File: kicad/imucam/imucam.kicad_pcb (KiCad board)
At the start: 4 copper layers, 52.3 x 76.2 mm, 158 parts, among them J1 JTAG, J2 EXTCAM, J3 NUCLEO_CN8, J4 NUCLEO_CN9, J5 NUCLEO_CN7, J6 NUCLEO_CN10, J7 HDMI, Q1 BSS214NW, Q2 BSS214NW, Q3 BSS214NW, Q4 BSS214NW, U1 TLV73310PDBVT, U10 NTS0308E, U11 PTN3366, U12 AP2331, U2 LIFCL-17-xSG72, U3 AT25SF081-SSHD-X, U4 MIC5365-2.8YD5, U5 AR0330CM1C00, U6 ICM20948, U7 TPS562200, U8 INA219AxDCN, U9 TPS562200, X1 ECS-2520MV-xxx-xx

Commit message: Ready to begin routing differential pairs
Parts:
- C1, C10, C12, C13, C14, C15, C16, C17, C18, C19, C20, C21, C22, C23, C24, C25, C26, C27, C28, C29, C3, C30, C31, C32, C33, C34, C4, C40, C41, C42, C43, C44, C45, C46, C47, C48, C49, C5, C50, C51, C52, C53, C6, C7, C74, C75, C9, FB1, FB2, FB3, FB4: moved to B.Cu
- U11: footprint Package_DFN_QFN:QFN-32-1EP_5x5mm_P0.5mm_EP3.6x3.6mm_ThermalVias -> Package_DFN_QFN:QFN-32-1EP_5x5mm_P0.5mm_EP3.6x3.6mm
- U2: footprint Package_DFN_QFN:QFN-72-1EP_10x10mm_P0.5mm_EP6x6mm_ThermalVias -> Package_DFN_QFN:QFN-72-1EP_10x10mm_P0.5mm_EP6x6mm
- U6: footprint Package_DFN_QFN:QFN-24-1EP_3x3mm_P0.4mm_EP1.75x1.6mm -> imucam:QFN-24-1EP_3x3mm_P0.4mm_EP1.75x1.6mm_NoDiePad
- moved C23 216.3 mm to (27.1, 62.5), turned to 180 degrees
- moved C22 205.5 mm to (21.4, 61.9), turned to 90 degrees
- moved C30 162.7 mm to (27.1, 58.5), turned to 180 degrees
- moved C1 160.0 mm to (27.1, 59.5), turned to 180 degrees
- moved C19 151.1 mm to (27.4, 53.0), turned to 180 degrees
- moved C24 149.2 mm to (22.8, 64.3)
- moved C3 147.4 mm to (27.1, 56.6), turned to 180 degrees
- moved C27 145.9 mm to (24.4, 55.2), turned to 270 degrees
- moved R27 145.7 mm to (6.71, 2.62)
- moved C9 144.4 mm to (25.8, 63.8), turned to 180 degrees
- moved C13 143.1 mm to (21.0, 55.2), turned to 270 degrees
- moved C26 141.8 mm to (27.4, 55.0), turned to 270 degrees
- moved C12 141.4 mm to (29.0, 57.7), turned to 90 degrees
- moved C25 139.8 mm to (27.1, 60.5), turned to 180 degrees
- moved C6 139.8 mm to (24.1, 60.8), turned to 90 degrees
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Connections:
- net Net-(C11-Pad1) renamed /FPGA/1V8A_PHY
- net Net-(C15-Pad1) renamed /FPGA/1V0A_PHY
- net Net-(C30-Pad1) renamed /FPGA/1V8A
- net Net-(C4-Pad1) renamed /FPGA/1V0A_PLL
- net Net-(C66-Pad1) renamed /hdmi/IN_D1+
- net Net-(C67-Pad1) renamed /hdmi/IN_D2+
- net Net-(C68-Pad1) renamed /hdmi/IN_D3+
- net Net-(C69-Pad1) renamed /hdmi/IN_D4+
- net Net-(C70-Pad1) renamed /hdmi/IN_D1-
- net Net-(C71-Pad1) renamed /hdmi/IN_D2-
- net Net-(C72-Pad1) renamed /hdmi/IN_D3-
- net Net-(C73-Pad1) renamed /hdmi/IN_D4-
- J3 pad 10: (no net) -> /nucleo/LED3
- J3 pad 6: (no net) -> /nucleo/LED1
- J3 pad 8: (no net) -> /nucleo/LED2
- J4 pad 14: (no net) -> /nucleo/IMU_SCK_3V3
- J4 pad 16: CAM_RESET_BAR -> /nucleo/IMU_CS_3V3
- J4 pad 18: (no net) -> /nucleo/IMU_SO_3V3
- J4 pad 19: HDMI_SCL -> SCL_3V3
- J4 pad 20: (no net) -> /nucleo/IMU_SI_3V3
- J4 pad 21: HDMI_SDA -> SDA_3V3
- J4 pad 22: (no net) -> /nucleo/IMU_INT_3V3
- J4 pad 24: HDMI_HPD -> (no net)
- J4 pad 26: HDMI_OE -> (no net)
- J4 pad 28: HDMI_DDC_EN -> (no net)
- J4 pad 29: HDMI_EQ0 -> (no net)
- J4 pad 30: HDMI_EQ1 -> (no net)
- J5 pad 11: /nucleo/IMU_INT_3V3 -> (no net)
- J5 pad 13: /nucleo/IMU_SI_3V3 -> (no net)
- J5 pad 15: /nucleo/IMU_SCK_3V3 -> (no net)
- J5 pad 17: /nucleo/IMU_CS_3V3 -> (no net)
- J5 pad 19: /nucleo/IMU_SO_3V3 -> (no net)
- J5 pad 2: SCL_3V3 -> (no net)
- J5 pad 4: SDA_3V3 -> (no net)
- J6 pad 12: (no net) -> HDMI_SDA
- J6 pad 13: (no net) -> HDMI_OE
- J6 pad 15: (no net) -> HDMI_DDC_EN
- J6 pad 19: /nucleo/LED3 -> HDMI_EQ0
- J6 pad 2: (no net) -> CAM_RESET_BAR
- J6 pad 21: /nucleo/LED2 -> HDMI_HPD
- J6 pad 23: /nucleo/LED1 -> HDMI_EQ1
- J6 pad 8: (no net) -> HDMI_SCL
- R18 pad 1: +5V -> /nucleo/5V_IN
- R18 pad 2: /nucleo/5V_IN -> +5V
- U10 pad 11: (no net) -> GND
- U2 pad 10: HDMI_D2_N -> HDMI_D2_P
- U2 pad 11: HDMI_D2_P -> HDMI_D2_N
- U2 pad 13: HDMI_D1_N -> HDMI_D1_P
- U2 pad 14: HDMI_D1_P -> HDMI_D1_N
- U2 pad 15: HDMI_D0_N -> HDMI_D0_P
- U2 pad 16: HDMI_D0_P -> HDMI_D0_N
- U3 pad 3: +3V3 -> (no net)
- U3 pad 7: +3V3 -> (no net)
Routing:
- net GND: track 0.00 -> 58.3 mm, vias 0 -> 17
- net +1V0: track 0.00 -> 39.8 mm, vias 0 -> 5
- net /FPGA/1V8A: track 0.00 -> 25.4 mm, vias 0 -> 4
- net +1V8: track 0.81 -> 23.2 mm, vias 0 -> 9
- net HDMI_D2_P: track 0.00 -> 15.4 mm
- net HDMI_D2_N: track 0.00 -> 14.8 mm
- net HDMI_D1_P: track 0.00 -> 12.6 mm
- net HDMI_D1_N: track 0.00 -> 12.0 mm
- net +2V8: track 0.00 -> 11.7 mm, vias 0 -> 3
- net HDMI_D0_P: track 0.00 -> 10.2 mm
- net HDMI_D0_N: track 0.00 -> 9.65 mm
- net +3V3: track 0.00 -> 9.00 mm, vias 0 -> 4
- net HDMI_CK_P: track 0.00 -> 7.72 mm
- net HDMI_CK_N: track 0.00 -> 7.43 mm
- net /FPGA/1V0A_PHY: track 0.00 -> 5.81 mm, vias 0 -> 1
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
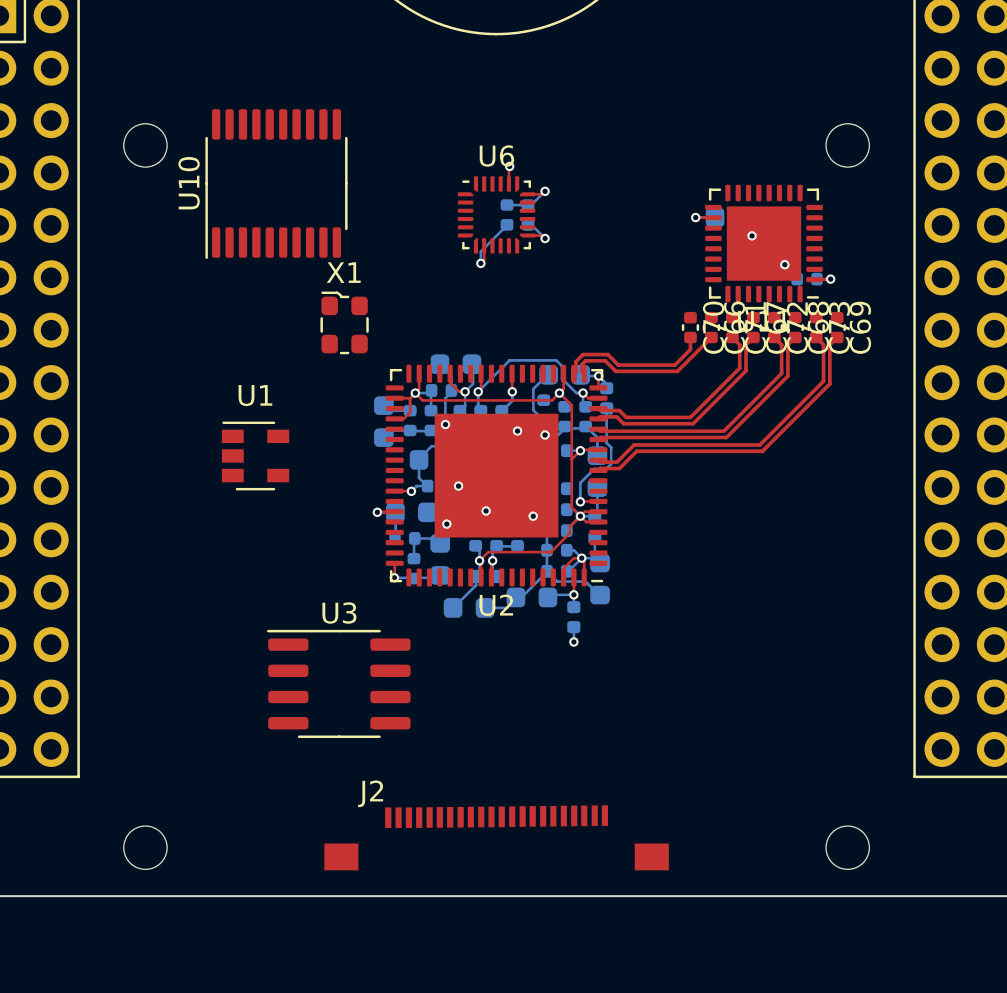
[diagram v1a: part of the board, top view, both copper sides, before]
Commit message: Routed first differential pairs
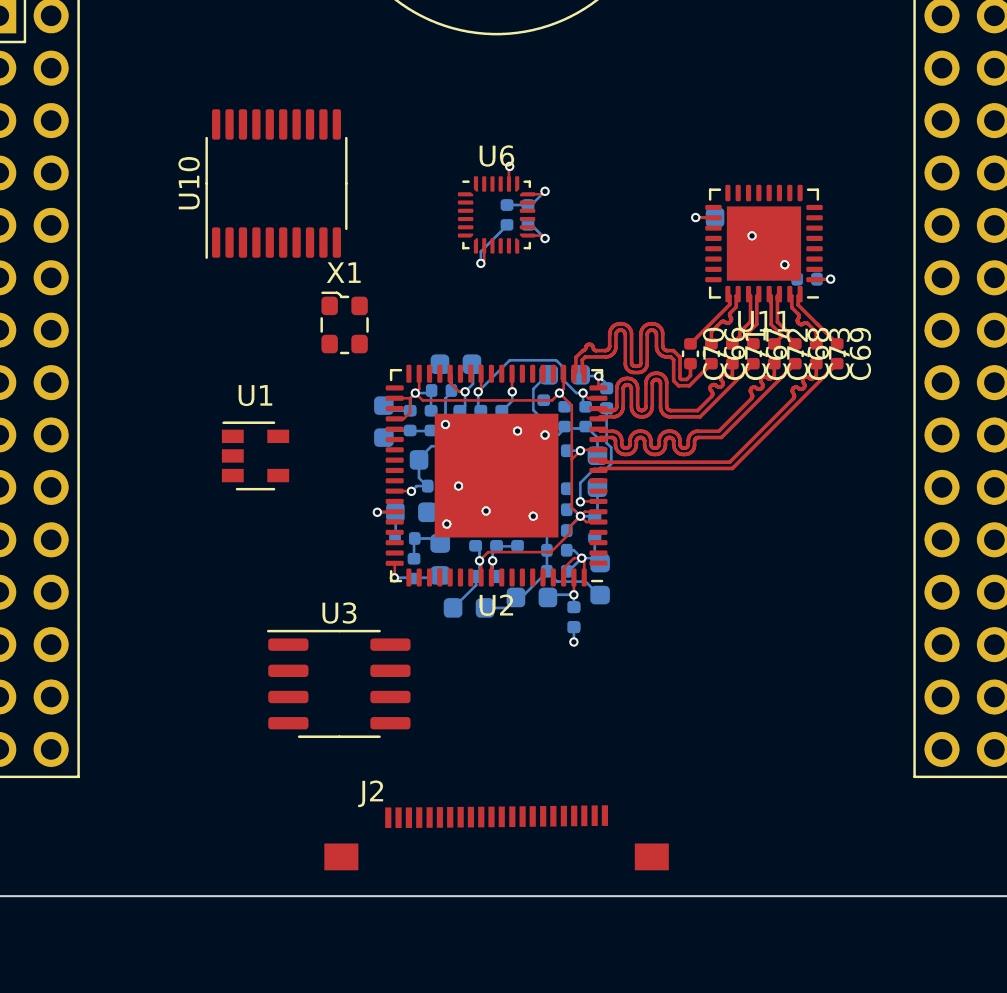
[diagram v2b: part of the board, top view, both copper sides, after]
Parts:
- removed H2: EXTCAM, imucam:Arducam_module_40mm
- moved C66 1.27 mm to (34.5, 51.9)
- moved C67 1.27 mm to (36.6, 51.9)
- moved C68 1.27 mm to (38.6, 51.9)
- moved C69 1.27 mm to (40.6, 51.9)
- moved C70 1.27 mm to (33.5, 51.9)
- moved C71 1.27 mm to (35.6, 51.9)
- moved C72 1.27 mm to (37.6, 51.9)
- moved C73 1.27 mm to (39.6, 51.9)
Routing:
- net HDMI_CK_N: track 7.43 -> 14.2 mm
- net HDMI_CK_P: track 7.72 -> 14.2 mm
- net HDMI_D0_N: track 9.65 -> 14.5 mm
- net HDMI_D0_P: track 10.2 -> 14.2 mm
- net /hdmi/IN_D1+: track 0.00 -> 3.29 mm
- net /hdmi/IN_D4-: track 0.00 -> 3.29 mm
- net /hdmi/IN_D1-: track 0.00 -> 3.24 mm
- net /hdmi/IN_D4+: track 0.00 -> 3.24 mm
- net /hdmi/IN_D3-: track 0.00 -> 3.13 mm
- net /hdmi/IN_D3+: track 0.00 -> 3.00 mm
- net /hdmi/IN_D2+: track 0.00 -> 2.82 mm
- net /hdmi/IN_D2-: track 0.00 -> 2.82 mm
- net HDMI_D1_N: track 12.0 -> 14.3 mm
- net HDMI_D1_P: track 12.6 -> 14.3 mm
- net HDMI_D2_P: track 15.4 -> 13.7 mm
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
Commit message: More routing
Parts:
- added H2: EXTCAM, imucam:Arducam_module_40mm, F.Cu at (24.1, 57.3)
- C35, C36, C37, C54, C62, C65, FB5, R31, R32, R33, R34, R35, R36, R37, R38, R39: moved to B.Cu
- moved R11 269.7 mm to (64.8, 44.5)
- moved R12 186.9 mm to (-19.3, 57.6), turned to 180 degrees
- moved C65 149.0 mm to (6.73, 55.5), turned to 90 degrees
- moved C37 84.9 mm to (16.8, 49.8)
- moved C36 84.2 mm to (16.8, 51.2)
- moved FB5 84.2 mm to (16.8, 48.8)
- moved C35 80.9 mm to (16.0, 67.6), turned to 270 degrees
- moved R39 59.0 mm to (27.6, 14.9), turned to 180 degrees
- moved C62 50.0 mm to (7.75, 55.5), turned to 270 degrees
- moved R34 41.6 mm to (34.7, 47.1), turned to 270 degrees
- moved C54 41.3 mm to (24.6, 45.2), turned to 90 degrees
- moved R31 35.2 mm to (39.2, 45.3), turned to 0 degrees
- moved R35 32.0 mm to (39.2, 44.3), turned to 0 degrees
- moved R38 31.8 mm to (27.1, 15.9), turned to 180 degrees
- moved R36 31.3 mm to (39.2, 49.3), turned to 0 degrees
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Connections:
- J6 pad 13: HDMI_OE -> HDMI_EQ0
- J6 pad 15: HDMI_DDC_EN -> HDMI_EQ1
- J6 pad 19: HDMI_EQ0 -> HDMI_HPD
- J6 pad 21: HDMI_HPD -> HDMI_DDC_EN
- J6 pad 23: HDMI_EQ1 -> HDMI_OE
- R25 pad 1: SDA_1V8 -> SCL_1V8
- R26 pad 1: SCL_1V8 -> SDA_1V8
- R29 pad 2: SCL_3V3 -> SDA_3V3
- R30 pad 2: SDA_3V3 -> SCL_3V3
- U10 pad 1: SCL_1V8 -> SDA_1V8
- U10 pad 13: /nucleo/IMU_SI_3V3 -> /nucleo/IMU_SCK_3V3
- U10 pad 14: /nucleo/IMU_SO_3V3 -> /nucleo/IMU_CS_3V3
- U10 pad 15: /nucleo/IMU_CS_3V3 -> /nucleo/IMU_SO_3V3
- U10 pad 16: /nucleo/IMU_SCK_3V3 -> /nucleo/IMU_SI_3V3
- U10 pad 18: SDA_3V3 -> SCL_3V3
- U10 pad 20: SCL_3V3 -> SDA_3V3
- U10 pad 3: SDA_1V8 -> SCL_1V8
- U10 pad 5: IMU_SCK -> IMU_SI
- U10 pad 6: IMU_CS -> IMU_SO
- U10 pad 7: IMU_SO -> IMU_CS
- U10 pad 8: IMU_SI -> IMU_SCK
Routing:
- net GND: track 58.3 -> 111.9 mm, vias 17 -> 41
- net /hdmi/D2_N: track 0.00 -> 49.8 mm, vias 0 -> 2
- net /hdmi/D2_P: track 0.00 -> 49.7 mm, vias 0 -> 2
- net /hdmi/D0_N: track 0.00 -> 49.7 mm, vias 0 -> 2
- net /hdmi/D0_P: track 0.00 -> 49.7 mm, vias 0 -> 2
- net /hdmi/CK_N: track 0.00 -> 49.4 mm, vias 0 -> 2
- net /hdmi/CK_P: track 0.00 -> 49.4 mm, vias 0 -> 2
- net /hdmi/D1_N: track 0.00 -> 49.4 mm, vias 0 -> 2
- net /hdmi/D1_P: track 0.00 -> 49.3 mm, vias 0 -> 2
- net Net-(J7-Pad15): track 0.00 -> 46.0 mm, vias 0 -> 2
- net Net-(J7-Pad16): track 0.00 -> 45.9 mm, vias 0 -> 2
- net CLK_24MHZ: track 0.00 -> 40.0 mm, vias 0 -> 2
- net Net-(J7-Pad19): track 0.00 -> 38.7 mm, vias 0 -> 2
- net +3V3: track 9.00 -> 37.1 mm, vias 4 -> 8
- net HDMI_OE: track 0.00 -> 24.3 mm, vias 0 -> 2
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- added copper zone on F.Cu, net +1V8
- added copper zone on F.Cu, net +3V3
- added copper zone on F.Cu, net +5V
- added copper zone on F.Cu, net GND
- added copper zone on B.Cu, net Net-(C57-Pad1)
- added copper zone on F.Cu, net Net-(C57-Pad1)
- added copper zone on B.Cu, net Net-(C63-Pad1)
- added copper zone on F.Cu, net Net-(C63-Pad1)
